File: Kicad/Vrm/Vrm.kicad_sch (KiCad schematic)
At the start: 32 parts, among them J1 Screw_Terminal_01x05, J2 AVR-JTAG-10, J3 Screw_Terminal_01x03, J4 Screw_Terminal_01x04, Q1 FMMT458TA - SOT23, SW1 Switch, U1 STM32F091RCTx, U2 LT1302, U3 LTC3631

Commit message: Final Schematic
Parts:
- U2: value LT1302 -> LT1302CS8
- renumbered C11 to C?, C10 to C?, C12 to C?, U3 to U1

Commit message: real changes
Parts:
- removed C?: 2.2uF, symbol Device:C
- removed L1, L2: 100uH, symbol pspice:INDUCTOR
- removed U1: LTC3631, Package_SO:Linear_MSOP-12-16-1EP_3x4mm_P0.5mm, symbol Regulator_Switching:LTC3638
- removed U2: LT1302CS8, Package_SO:Linear_MSOP-12-16-1EP_3x4mm_P0.5mm, symbol Regulator_Switching:LTC3638
- added C10: 10uF, symbol Device:C
- added U1: R-78E5_0-0_5, digikey-footprints:SIP-3_P2.54mm, symbol dk_DC-DC-Converters:R-78E5_0-0_5
- added U2: R-78E3.3-0.5, Converter_DCDC:Converter_DCDC_RECOM_R-78E-0.5_THT, symbol Regulator_Switching:R-78E3.3-0.5
- C8: value 2.2uF -> 10uF
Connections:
- net +7.5V: now also C1.2, C2.2, U1.1 (VDD), U2.1 (IN)
- net 3.3V: now also C8.2, U1.3 (OUT); no longer C1.1
- net 5V: now also C10.2, U2.3 (OUT); no longer C2.1
- net GND: now also C2.1, C10.1, U1.2 (GND), U2.2 (GND); no longer C1.2, C2.2, C8.2
- net +5V: no longer names the net of C8.1
- net +5V: now also C1.1

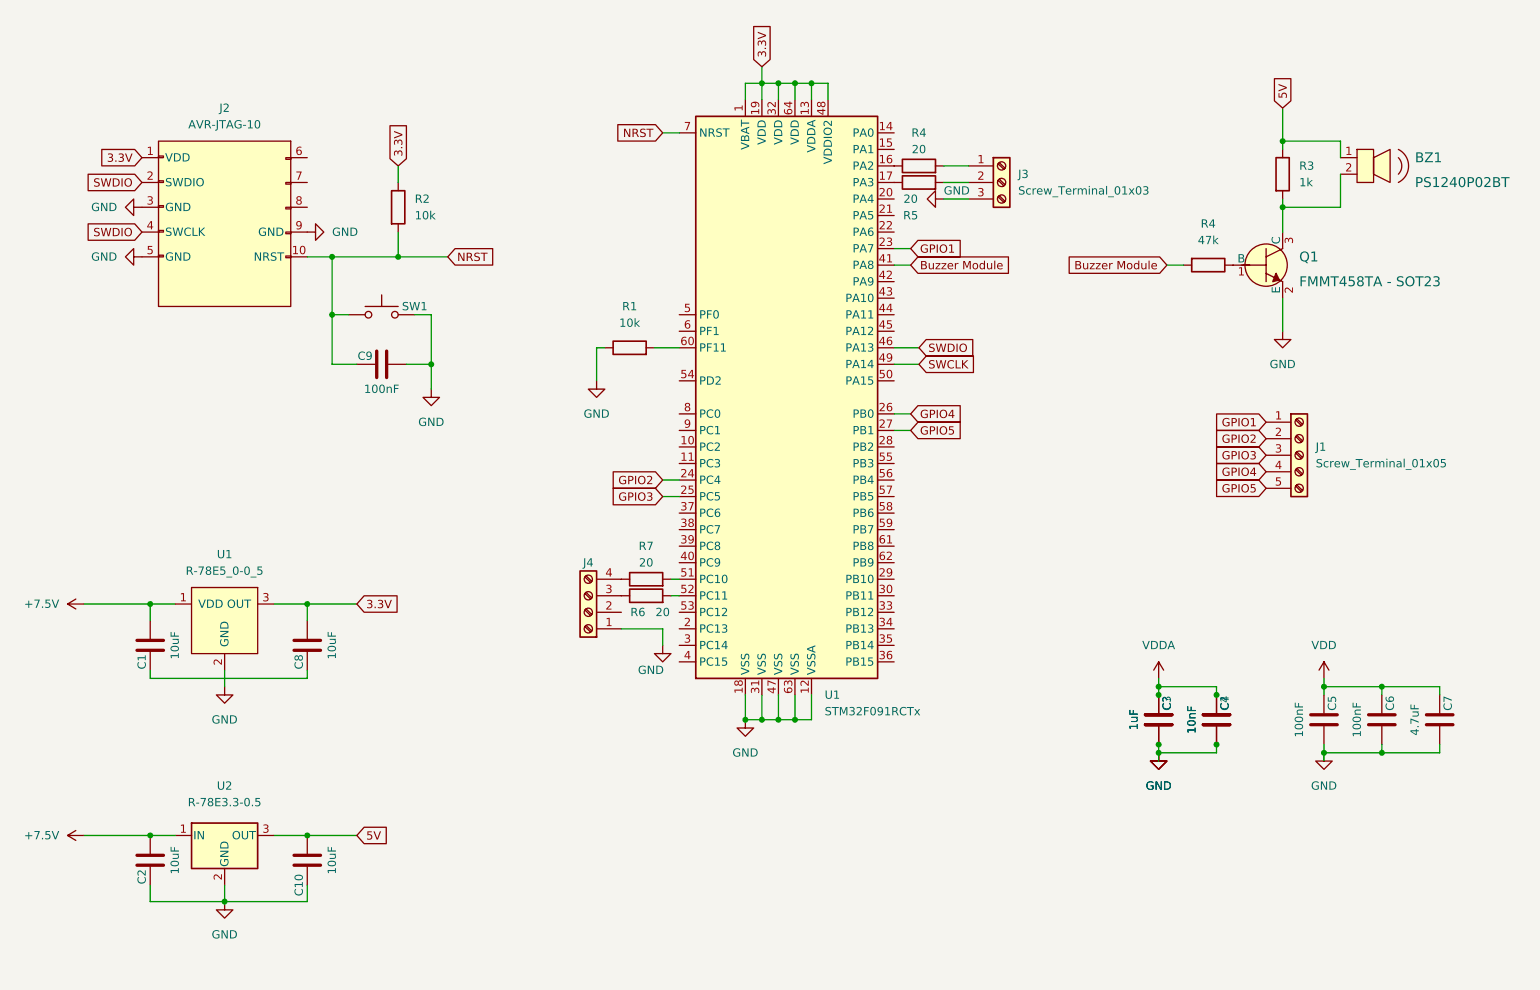
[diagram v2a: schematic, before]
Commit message: Added power modules to PCB
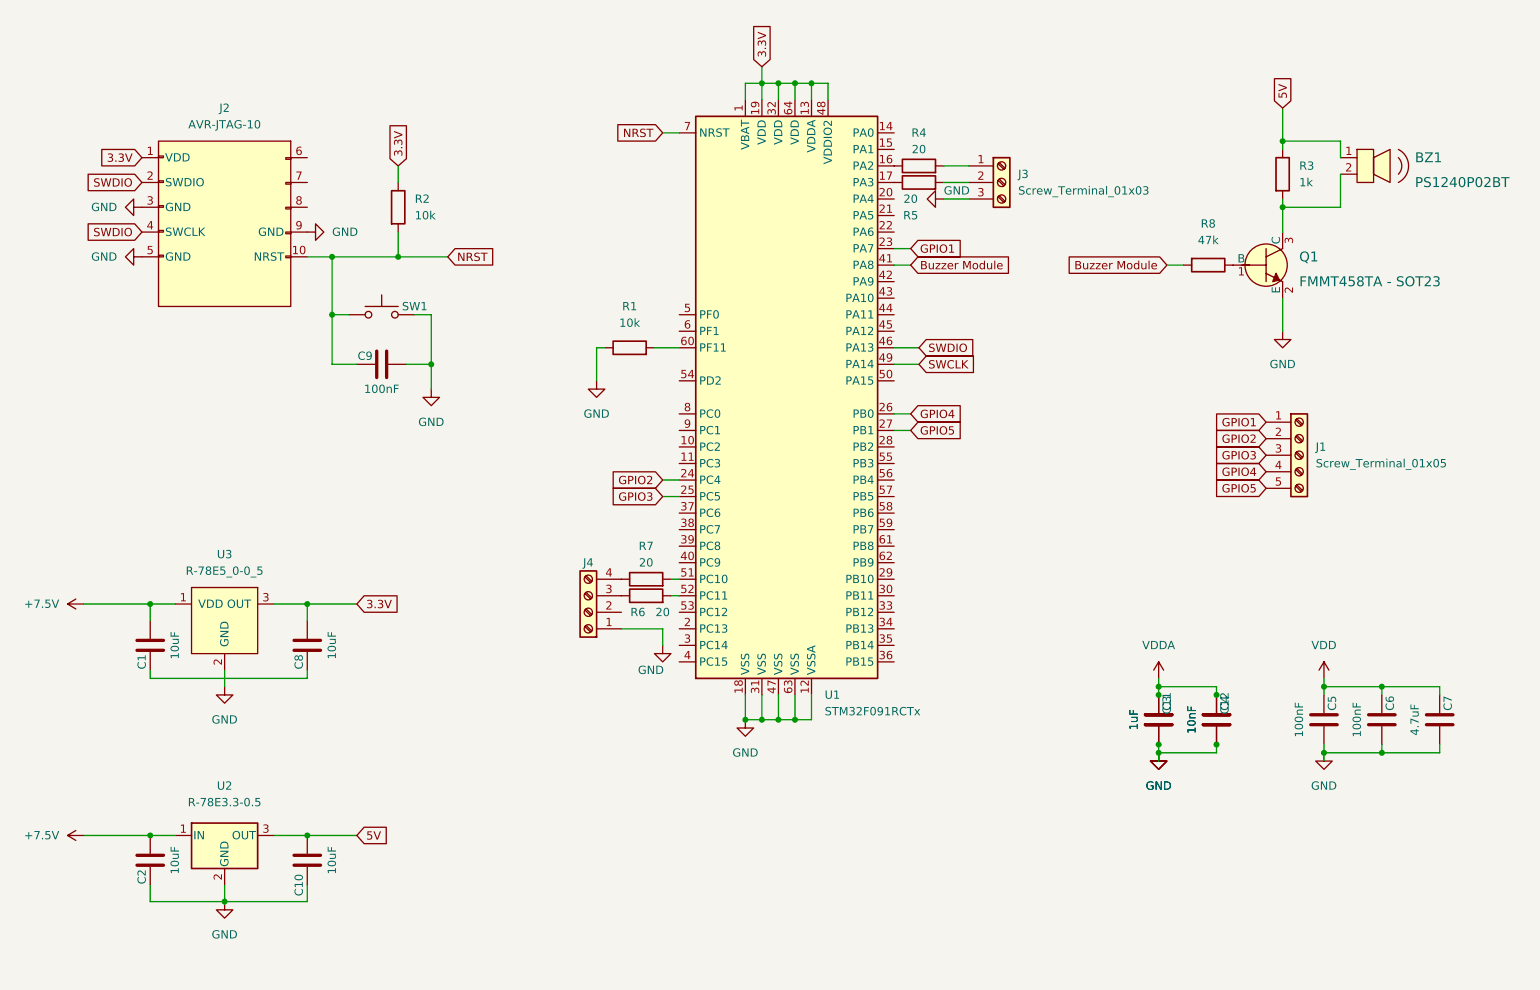
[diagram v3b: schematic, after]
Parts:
- gave numbers to parts that had none: 2
- renumbered R4 to R8, U1 to U3

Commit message: Last minute fixes from manlab
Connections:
- net GND: now also C1.1, C8.1
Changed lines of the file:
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@@
   (junction (at 86.36 60.96) (diameter 0) (color 0 0 0 0)
   )
+  (junction (at 59.69 125.73) (diameter 0) (color 0 0 0 0)
+  )
   (junction (at 142.24 132.08) (diameter 0) (color 0 0 0 0)
   )
@@
     (stroke (width 0) (type default) (color 0 0 0 0))
   )
+  (wire (pts (xy 59.69 125.73) (xy 72.39 125.73))
+    (stroke (width 0) (type default) (color 0 0 0 0))
+  )
   (wire (pts (xy 116.84 74.93) (xy 116.84 80.01))
     (stroke (width 0) (type default) (color 0 0 0 0))
@@
     (stroke (width 0) (type default) (color 0 0 0 0))
   )
+  (wire (pts (xy 59.69 125.73) (xy 59.69 127))
+    (stroke (width 0) (type default) (color 0 0 0 0))
+  )
   (wire (pts (xy 222.25 52.07) (xy 222.25 53.34))
     (stroke (width 0) (type default) (color 0 0 0 0))
@@
     (stroke (width 0) (type default) (color 0 0 0 0))
   )
+  (wire (pts (xy 48.26 125.73) (xy 59.69 125.73))
+    (stroke (width 0) (type default) (color 0 0 0 0))
+  )
   (wire (pts (xy 91.44 77.47) (xy 91.44 81.28))
     (stroke (width 0) (type default) (color 0 0 0 0))
@@
     (stroke (width 0) (type default) (color 0 0 0 0))
   )
-  (wire (pts (xy 48.26 125.73) (xy 72.39 125.73))
-    (stroke (width 0) (type default) (color 0 0 0 0))
-  )
   (wire (pts (xy 48.26 160.02) (xy 59.69 160.02))
     (stroke (width 0) (type default) (color 0 0 0 0))
@@
     (stroke (width 0) (type default) (color 0 0 0 0))
   )
-  (wire (pts (xy 59.69 124.46) (xy 59.69 127))
-    (stroke (width 0) (type default) (color 0 0 0 0))
-  )
+  (wire (pts (xy 59.69 124.46) (xy 59.69 125.73))
+    (stroke (width 0) (type default) (color 0 0 0 0))
+  )
